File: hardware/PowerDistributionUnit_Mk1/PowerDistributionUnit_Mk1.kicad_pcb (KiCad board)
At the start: 4 copper layers, 80.4 x 206 mm, 767 parts, among them J1 XT-30, J10 Logic Analyzer, J11 Logic Analyzer, J12 Logic Analyzer, J13 Logic Analyzer, J2 Molex_NanoFit_2x8, J3 Molex_NanoFit_1x6, J4 Molex_NanoFit_1x2, J5 Molex_NanoFit_1x2, J6 Conn_01x01, J8 Molex_NanoFit_1x2, J9 Molex_NanoFit_1x2, Q1 NVMFWS1D7N04XMT1G, Q2 NVMFWS1D7N04XMT1G, SW1 JS202011SCQN, U1 LeaderSOM, U10 74LVC594APW,118, U11 TPS27SA08CQPWPRQ1, U12 TPS27SA08CQPWPRQ1, U13 TPS27SA08CQPWPRQ1, U14 TPS27SA08CQPWPRQ1, U15 TPS27SA08CQPWPRQ1, U16 TPS27SA08CQPWPRQ1, U17 TPS27SA08CQPWPRQ1, U18 TPS27SA08CQPWPRQ1, U19 TPS27SA08CQPWPRQ1, U2 LM74502HDDFR, U20 TPS27SA08CQPWPRQ1, U21 TPS27SA08CQPWPRQ1, U22 MCP23S17-E/SO, U23 ADS131M08QPBSRQ1, U24 ADS131M08QPBSRQ1, U25 NL17SZS11DFT2G-Q, U26 TLV9002QDRQ1, U27 74LVC594APW,118, U28 74LVC594APW,118, U29 74AUP1G04GW-Q100H, U3 TPS27SA08CQPWPRQ1, U30 NL27WZ17DFT2G-Q, U31 74LVC594APW,118, U32 ACS37042KLHBLT-010B3, U33 ACS37042KLHBLT-010B3, U34 ACS37042KLHBLT-010B3, U35 ACS37042KLHBLT-010B3, U36 ACS37042KLHBLT-010B3, U37 ACS37042KLHBLT-010B3, U38 ACS37042KLHBLT-010B3, U39 ACS37042KLHBLT-010B3, U4 TPS27SA08CQPWPRQ1, U40 ACS37042KLHBLT-010B3, U41 ACS37042KLHBLT-010B3, U42 ACS37042KLHBLT-010B3, U43 ACS37042KLHBLT-010B3, U44 ACS37042KLHBLT-010B3, U45 ACS37042KLHBLT-010B3, U46 ACS37042KLHBLT-010B3, U47 ACS37042KLHBLT-010B3, U5 TPS27SA08CQPWPRQ1, U6 TPS27SA08CQPWPRQ1, U7 74LVC594APW,118, U8 74LVC594APW,118, U9 TPS27SA08CQPWPRQ1, Y1 ABM3-8.000MHZ-D2Y-T, Y2 ABM3-8.000MHZ-D2Y-T

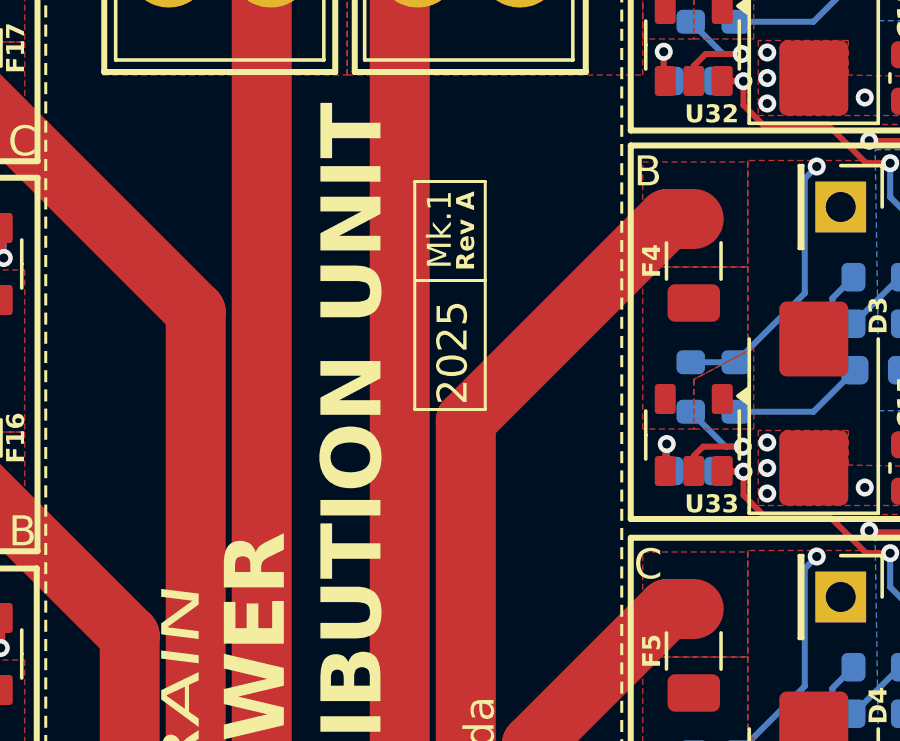
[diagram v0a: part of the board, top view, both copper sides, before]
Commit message: update rev and year label
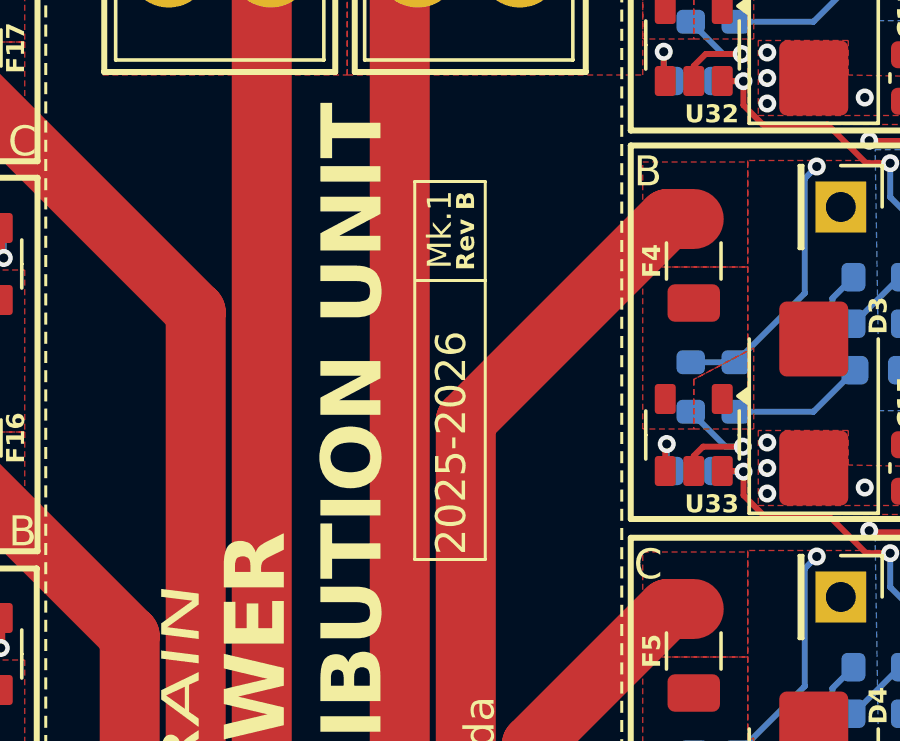
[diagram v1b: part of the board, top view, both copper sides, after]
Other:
- board text added: "2025-2026"
- board text added: "Rev B"
- board text removed: "2025"
- board text removed: "Rev A"
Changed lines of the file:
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@@
 	(gr_rect
 		(start 154.8 63.95)
-		(end 157.15 71.55)
+		(end 157.15 76.55)
 		(stroke
 			(width 0.1)
@@
 		)
 	)
-	(gr_text "Rev A"
+	(gr_text "Rev B"
 		(at 156.85 65.6 90)
 		(layer "F.SilkS")
@@
 		)
 	)
-	(gr_text "2025"
-		(at 156.65 71.4 90)
+	(gr_text "2025-2026"
+		(at 156.6 76.4 90)
 		(layer "F.SilkS")
 		(effects
